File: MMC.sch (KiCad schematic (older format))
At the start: 53 parts, among them SW2 SW_Push, SW3 SW_Push, U2 LPC1776FET180,551, Y5 XTAL_8MHZ_TXC_7A-8.000MAAE-T

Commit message: DDR terminations changed, HTML BoM with variant added
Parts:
- C92, C93, Y5: config (none) -> dnf

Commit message: SW2 placement changed, BOM cleared, FPGA boot, less ERC errors and wornings
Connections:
- wire segments 245 -> 246
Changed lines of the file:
@@
 	8400 9600 8150 9600
 Wire Wire Line
-	8150 9600 8150 8100
+	8150 9600 8150 8800
 Wire Wire Line
 	8150 8100 8400 8100
@@
 	0    1    1    0
 $EndComp
+$Comp
+L power:PWR_FLAG #FLG?
+U 1 1 5D5D63E5
+P 8150 8800
+AR Path="/5BABAC65/5D5D63E5" Ref="#FLG?"  Part="1"
+AR Path="/5BCEDA39/5D5D63E5" Ref="#FLG0138"  Part="1"
+F 0 "#FLG0138" H 8150 8875 50  0001 C CNN
+F 1 "PWR_FLAG" H 8150 8973 50  0000 C CNN
+F 2 "" H 8150 8800 50  0001 C CNN
+F 3 "~" H 8150 8800 50  0001 C CNN
+	1    8150 8800
+	0    -1   -1   0
+$EndComp
+Connection ~ 8150 8800
+Wire Wire Line
+	8150 8800 8150 8100
+$Comp
+L power:PWR_FLAG #FLG?
+U 1 1 5D666D50
+P 8250 7900
+AR Path="/5BABAC65/5D666D50" Ref="#FLG?"  Part="1"
+AR Path="/5BCEDA39/5D666D50" Ref="#FLG0141"  Part="1"
+F 0 "#FLG0141" H 8250 7975 50  0001 C CNN
+F 1 "PWR_FLAG" H 8250 8073 50  0000 C CNN
+F 2 "" H 8250 7900 50  0001 C CNN
+F 3 "~" H 8250 7900 50  0001 C CNN
+	1    8250 7900
+	0    -1   -1   0
+$EndComp
 Wire Bus Line

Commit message: BOM updated, 25MHz clock level fixed
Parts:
- removed C92: CC0402_22PF_50V_5%_C0G, CAPC1005X55N, symbol Capacitors_SMD:CC0402_22PF_50V_5%_C0G
- added C92: CC0402_150PF_50V_5%_C0G, CAPC1005X55N, symbol Capacitors_SMD:CC0402_150PF_50V_5%_C0G
- R132: config (none) -> dnf
- SW3: value SW_Push -> KSS241GLFS
- U2: symbol AMC_FMC_Carrier-PcbDoc-rescue:LPC1776FET180,551-lpc1776fet180,551 -> AMC_FMC_Carrier-PcbDoc-rescue:LPC1776FET180,551-lpc1776fet180,551-AMC_FMC_Carrier-PcbDoc-rescue
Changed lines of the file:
@@
 $EndDescr
 $Comp
-L AMC_FMC_Carrier-PcbDoc-rescue:LPC1776FET180,551-lpc1776fet180,551 U?
+L AMC_FMC_Carrier-PcbDoc-rescue:LPC1776FET180,551-lpc1776fet180,551-AMC_FMC_Carrier-PcbDoc-rescue U?
 U 5 1 5BDFEB43
 P 8600 7800
@@
 $EndComp
 $Comp
-L AMC_FMC_Carrier-PcbDoc-rescue:LPC1776FET180,551-lpc1776fet180,551 U?
+L AMC_FMC_Carrier-PcbDoc-rescue:LPC1776FET180,551-lpc1776fet180,551-AMC_FMC_Carrier-PcbDoc-rescue U?
 U 1 1 5BE07B67
 P 4550 850
@@
 $EndComp
 $Comp
-L AMC_FMC_Carrier-PcbDoc-rescue:LPC1776FET180,551-lpc1776fet180,551 U?
+L AMC_FMC_Carrier-PcbDoc-rescue:LPC1776FET180,551-lpc1776fet180,551-AMC_FMC_Carrier-PcbDoc-rescue U?
 U 2 1 5BE0A46F
 P 13050 4700
@@
 $EndComp
 $Comp
-L AMC_FMC_Carrier-PcbDoc-rescue:LPC1776FET180,551-lpc1776fet180,551 U?
+L AMC_FMC_Carrier-PcbDoc-rescue:LPC1776FET180,551-lpc1776fet180,551-AMC_FMC_Carrier-PcbDoc-rescue U?
 U 4 1 5BE0D06F
 P 2750 8300
@@
 F 40 "Resistors SMD" H 2550 5780 60  0001 L CNN "Library Name"
 F 41 "This work is licensed under the Creative Commons CC-BY-SA 4.0 License. To the extent that circuit schematics that use Licensed Material can be considered to be ‘Adapted Material’, then the copyright holder waives article 3.b of the license with respect to these schematics." H 2550 5690 60  0001 L CNN "License"
+F 42 "dnf" V 2850 9650 50  0000 C CNN "config"
 	1    2550 9500
 	0    1    1    0
@@
 F 1 "SW_Push" H 10050 4944 50  0000 C CNN
 F 2 "Switches:PB_ALPS_SKHHLQA010" H 10050 4950 50  0001 C CNN
-F 3 "~" H 10050 4950 50  0001 C CNN
+F 3 "PB_ALPS_SKHHLQA010" H 10050 4950 50  0001 C CNN
 	1    10050 4750
 	1    0    0    -1
@@
 	3900 7150 4350 7150
 $Comp
-L AMC_FMC_Carrier-PcbDoc-rescue:LPC1776FET180,551-lpc1776fet180,551 U?
+L AMC_FMC_Carrier-PcbDoc-rescue:LPC1776FET180,551-lpc1776fet180,551-AMC_FMC_Carrier-PcbDoc-rescue U?
 U 3 1 5BE04771
 P 13050 650
@@
 NoConn ~ 12850 3450
 NoConn ~ 4350 6750
-$Comp
-L Switch:SW_Push SW?
-U 1 1 5CF2A4CC
-P 10050 5150
-AR Path="/5CF2A4CC" Ref="SW?"  Part="1"
-AR Path="/5BCEDA39/5CF2A4CC" Ref="SW3"  Part="1"
-F 0 "SW3" H 10050 5435 50  0000 C CNN
-F 1 "SW_Push" H 10050 5344 50  0000 C CNN
-F 2 "AG5300_2:KSS241GLFS" H 10050 5350 50  0001 C CNN
-F 3 "~" H 10050 5350 50  0001 C CNN
-	1    10050 5150
-	1    0    0    -1
-$EndComp
 Wire Wire Line
 	9850 4750 9850 5150
@@
 $EndComp
 $Comp
-L Capacitors_SMD:CC0402_22PF_50V_5%_C0G C92
-U 1 1 5CAC322E
+L power:PWR_FLAG #FLG?
+U 1 1 5D5D63E5
+P 8150 8800
+AR Path="/5BABAC65/5D5D63E5" Ref="#FLG?"  Part="1"
+AR Path="/5BCEDA39/5D5D63E5" Ref="#FLG0138"  Part="1"
+F 0 "#FLG0138" H 8150 8875 50  0001 C CNN
+F 1 "PWR_FLAG" H 8150 8973 50  0000 C CNN
+F 2 "" H 8150 8800 50  0001 C CNN
+F 3 "~" H 8150 8800 50  0001 C CNN
+	1    8150 8800
+	0    -1   -1   0
+$EndComp
+Connection ~ 8150 8800
+Wire Wire Line
+	8150 8800 8150 8100
+$Comp
+L power:PWR_FLAG #FLG?
+U 1 1 5D666D50
+P 8250 7900
+AR Path="/5BABAC65/5D666D50" Ref="#FLG?"  Part="1"
+AR Path="/5BCEDA39/5D666D50" Ref="#FLG0141"  Part="1"
+F 0 "#FLG0141" H 8250 7975 50  0001 C CNN
+F 1 "PWR_FLAG" H 8250 8073 50  0000 C CNN
+F 2 "" H 8250 7900 50  0001 C CNN
+F 3 "~" H 8250 7900 50  0001 C CNN
+	1    8250 7900
+	0    -1   -1   0
+$EndComp
+Wire Bus Line
+	11600 7200 11600 7400
+Wire Bus Line
+	12150 6100 12150 6400
+Wire Bus Line
+	10450 2900 10450 3650
+$Comp
+L Capacitors_SMD:CC0402_150PF_50V_5%_C0G C92
+U 1 1 5CFB3911
 P 1100 9550
 F 0 "C92" V 1204 9660 50  0000 L CNN
-F 1 "CC0402_22PF_50V_5%_C0G" H 1100 9290 60  0001 L CNN
+F 1 "CC0402_150PF_50V_5%_C0G" H 1100 9290 60  0001 L CNN
 F 2 "CAPC1005X55N" H 1100 8480 60  0001 L CNN
-F 3 "\\\\cern.ch\\dfs\\Applications\\Altium\\Datasheets\\CC0805_C0G_KEMET_(Commercial Grade).pdf" H 1100 9110 60  0001 L CNN
-F 4 "22pF" V 1295 9660 50  0000 L CNN "~"
-F 5 "CC0402_22PF_50V_5%_C0G" H 1100 9020 60  0001 L CNN "Part Number"
+F 3 "" H 1100 9110 60  0001 L CNN
+F 4 "150pF" V 1295 9660 50  0000 L CNN "~"
+F 5 "CC0402_150PF_50V_5%_C0G" H 1100 9020 60  0001 L CNN "Part Number"
 F 6 "Capacitor - non polarized" H 1100 8930 60  0001 L CNN "Library Ref"
 F 7 "SchLib\\Capacitors.SchLib" H 1100 8840 60  0001 L CNN "Library Path"
@@
 F 13 "CAPC1005X55N" H 1100 8210 60  0001 L CNN "Footprint Ref"
 F 14 "~~" H 1100 8120 60  0001 L CNN "PackageDescription"
-F 15 "22pF" H 1100 8030 60  0001 L CNN "Val"
+F 15 "150pF" H 1100 8030 60  0001 L CNN "Val"
 F 16 "Preferred" H 1100 7940 60  0001 L CNN "Status"
 F 17 "~~" H 1100 7850 60  0001 L CNN "Status Comment"
@@
 F 21 "SMD Multilayer Chip Ceramic Capacitor" H 1100 7490 60  0001 L CNN "Part Description"
 F 22 "GENERIC" H 1100 7400 60  0001 L CNN "Manufacturer"
-F 23 "CC0402_22PF_50V_5%_C0G" H 1100 7310 60  0001 L CNN "Manufacturer Part Number"
+F 23 "CC0402_150PF_50V_5%_C0G" H 1100 7310 60  0001 L CNN "Manufacturer Part Number"
 F 24 "0402" H 1100 7220 60  0001 L CNN "Case"
 F 25 "Yes" H 1100 7130 60  0001 L CNN "Mounted"
@@
 F 31 "~~" H 1100 6590 60  0001 L CNN "ComponentHeight"
 F 32 "KEMET" H 1100 6500 60  0001 L CNN "Manufacturer1 Example"
-F 33 "C0402C220J5GACTU" H 1100 6410 60  0001 L CNN "Manufacturer1 Part Number"
+F 33 "C0402C151J5GACTU" H 1100 6410 60  0001 L CNN "Manufacturer1 Part Number"
 F 34 "0.55mm" H 1100 6320 60  0001 L CNN "Manufacturer1 ComponentHeight"
 F 35 "\\\\cern.ch\\dfs\\Applications\\Altium\\Datasheets\\CC0805_C0G_KEMET_(Commercial Grade).pdf" H 1100 6230 60  0001 L CNN "HelpURL"
 F 36 "CERN DEM JLC" H 1100 6140 60  0001 L CNN "Author"
 F 37 "12/03/07 00:00:00" H 1100 6050 60  0001 L CNN "CreateDate"
-F 38 "12/03/07 00:00:00" H 1100 5960 60  0001 L CNN "LatestRevisionDate"
+F 38 "04/22/15 00:00:00" H 1100 5960 60  0001 L CNN "LatestRevisionDate"
 F 39 "Capacitors SMD" H 1100 5870 60  0001 L CNN "Library Name"
 F 40 "This work is licensed under the Creative Commons CC-BY-SA 4.0 License. To the extent that circuit schematics that use Licensed Material can be considered to be ‘Adapted Material’, then the copyright holder waives article 3.b of the license with respect to these schematics." H 1100 5780 60  0001 L CNN "License"
-F 41 "dnf" V 1400 9700 50  0000 C CNN "config"
 	1    1100 9550
 	0    1    1    0
 $EndComp
 $Comp
-L power:PWR_FLAG #FLG?
-U 1 1 5D5D63E5
-P 8150 8800
-AR Path="/5BABAC65/5D5D63E5" Ref="#FLG?"  Part="1"
-AR Path="/5BCEDA39/5D5D63E5" Ref="#FLG0138"  Part="1"
-F 0 "#FLG0138" H 8150 8875 50  0001 C CNN
-F 1 "PWR_FLAG" H 8150 8973 50  0000 C CNN
-F 2 "" H 8150 8800 50  0001 C CNN
-F 3 "~" H 8150 8800 50  0001 C CNN
-	1    8150 8800
-	0    -1   -1   0
-$EndComp
-Connection ~ 8150 8800
-Wire Wire Line
-	8150 8800 8150 8100
-$Comp
-L power:PWR_FLAG #FLG?
-U 1 1 5D666D50
-P 8250 7900
-AR Path="/5BABAC65/5D666D50" Ref="#FLG?"  Part="1"
-AR Path="/5BCEDA39/5D666D50" Ref="#FLG0141"  Part="1"
-F 0 "#FLG0141" H 8250 7975 50  0001 C CNN
-F 1 "PWR_FLAG" H 8250 8073 50  0000 C CNN
-F 2 "" H 8250 7900 50  0001 C CNN
-F 3 "~" H 8250 7900 50  0001 C CNN
-	1    8250 7900
-	0    -1   -1   0
+L Switch:SW_Push SW?
+U 1 1 5CF2A4CC
+P 10050 5150
+AR Path="/5CF2A4CC" Ref="SW?"  Part="1"
+AR Path="/5BCEDA39/5CF2A4CC" Ref="SW3"  Part="1"
+F 0 "SW3" H 10050 5435 50  0000 C CNN
+F 1 "KSS241GLFS" H 10050 5344 50  0001 C CNN
+F 2 "AG5300_2:KSS241GLFS" H 10050 5350 50  0001 C CNN
+F 3 "KSS241GLFS" H 10050 5350 50  0001 C CNN
+	1    10050 5150
+	1    0    0    -1
 $EndComp
-Wire Bus Line
-	11600 7200 11600 7400
-Wire Bus Line
-	12150 6100 12150 6400
-Wire Bus Line
-	10450 2900 10450 3650
 $EndSCHEMATC

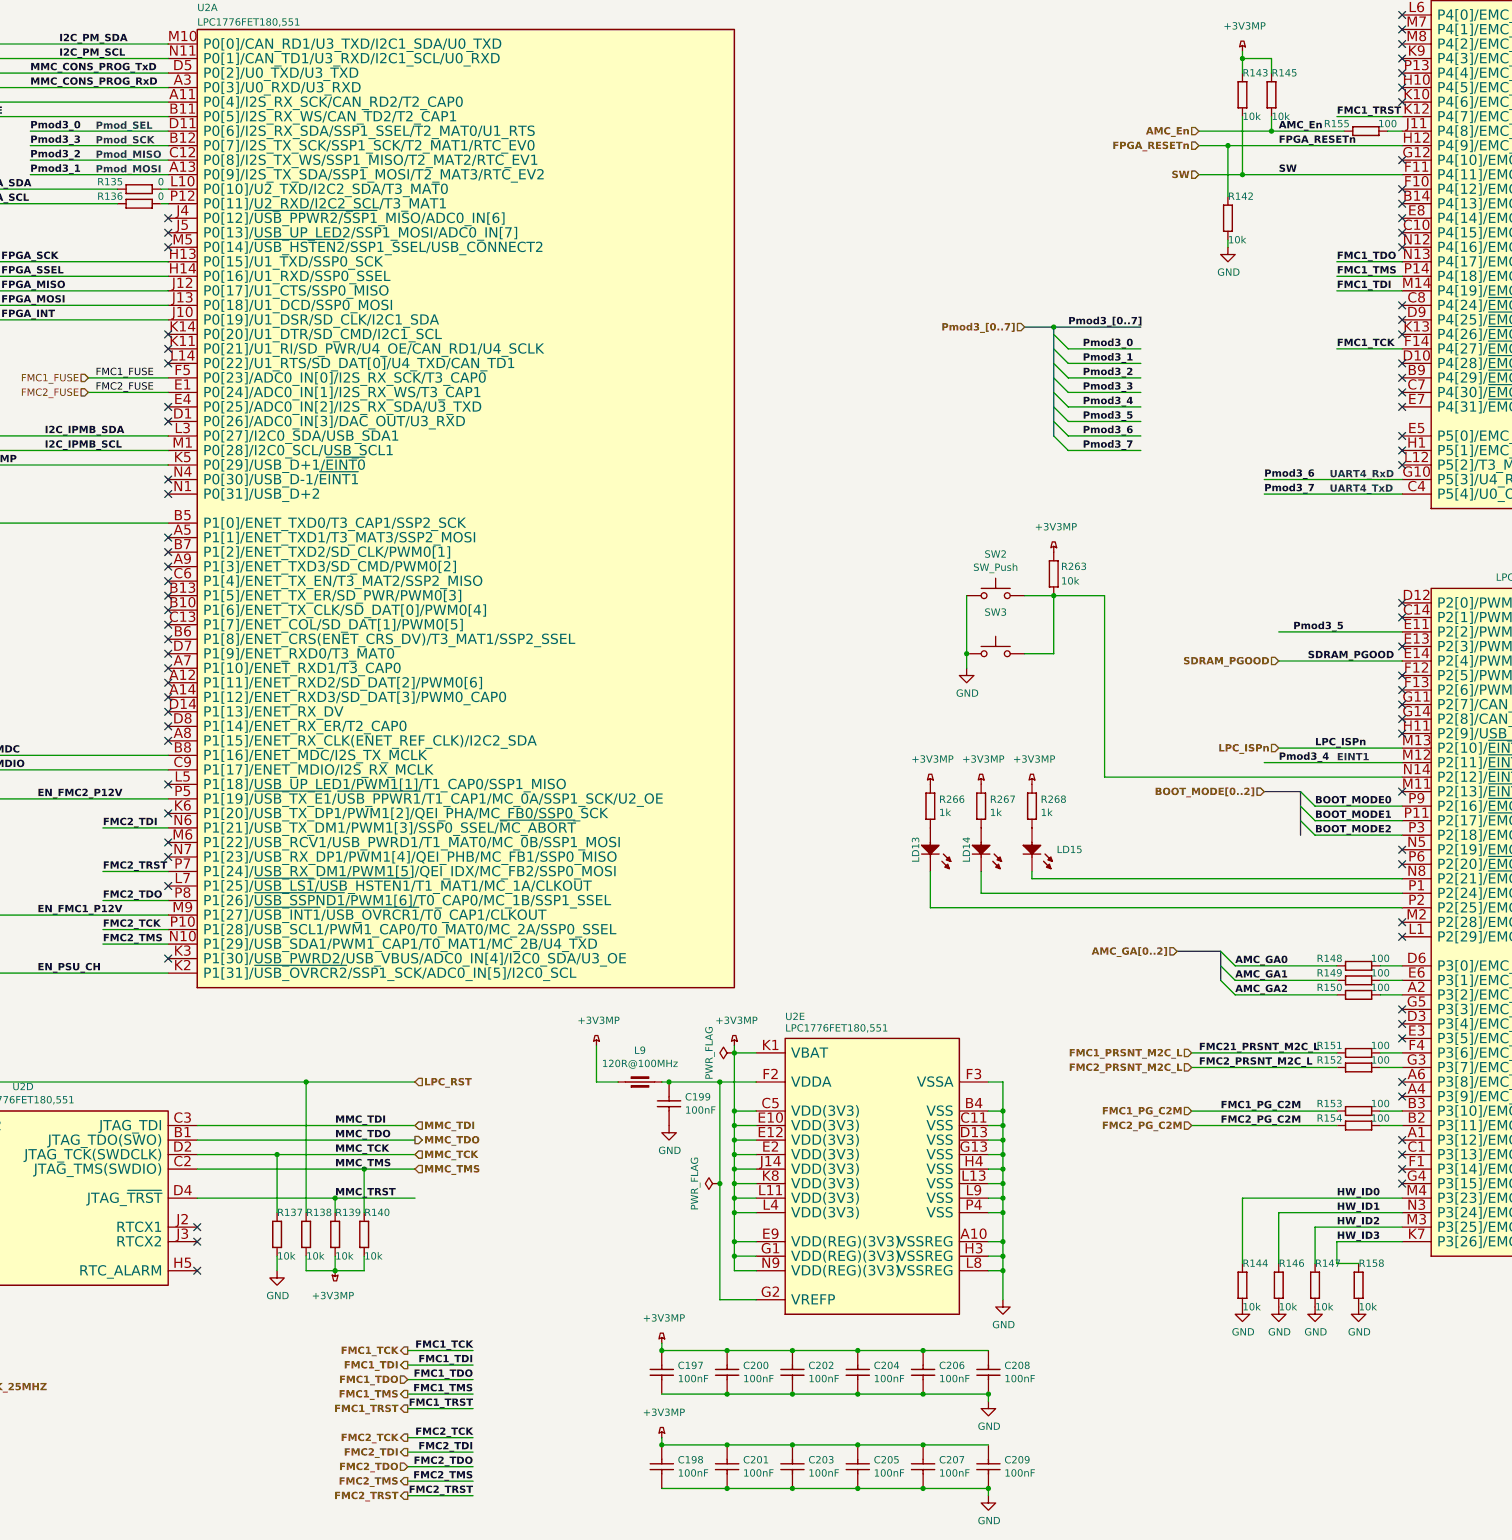
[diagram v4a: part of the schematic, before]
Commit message: new FMC JTAG chain connected to MMC GPIO
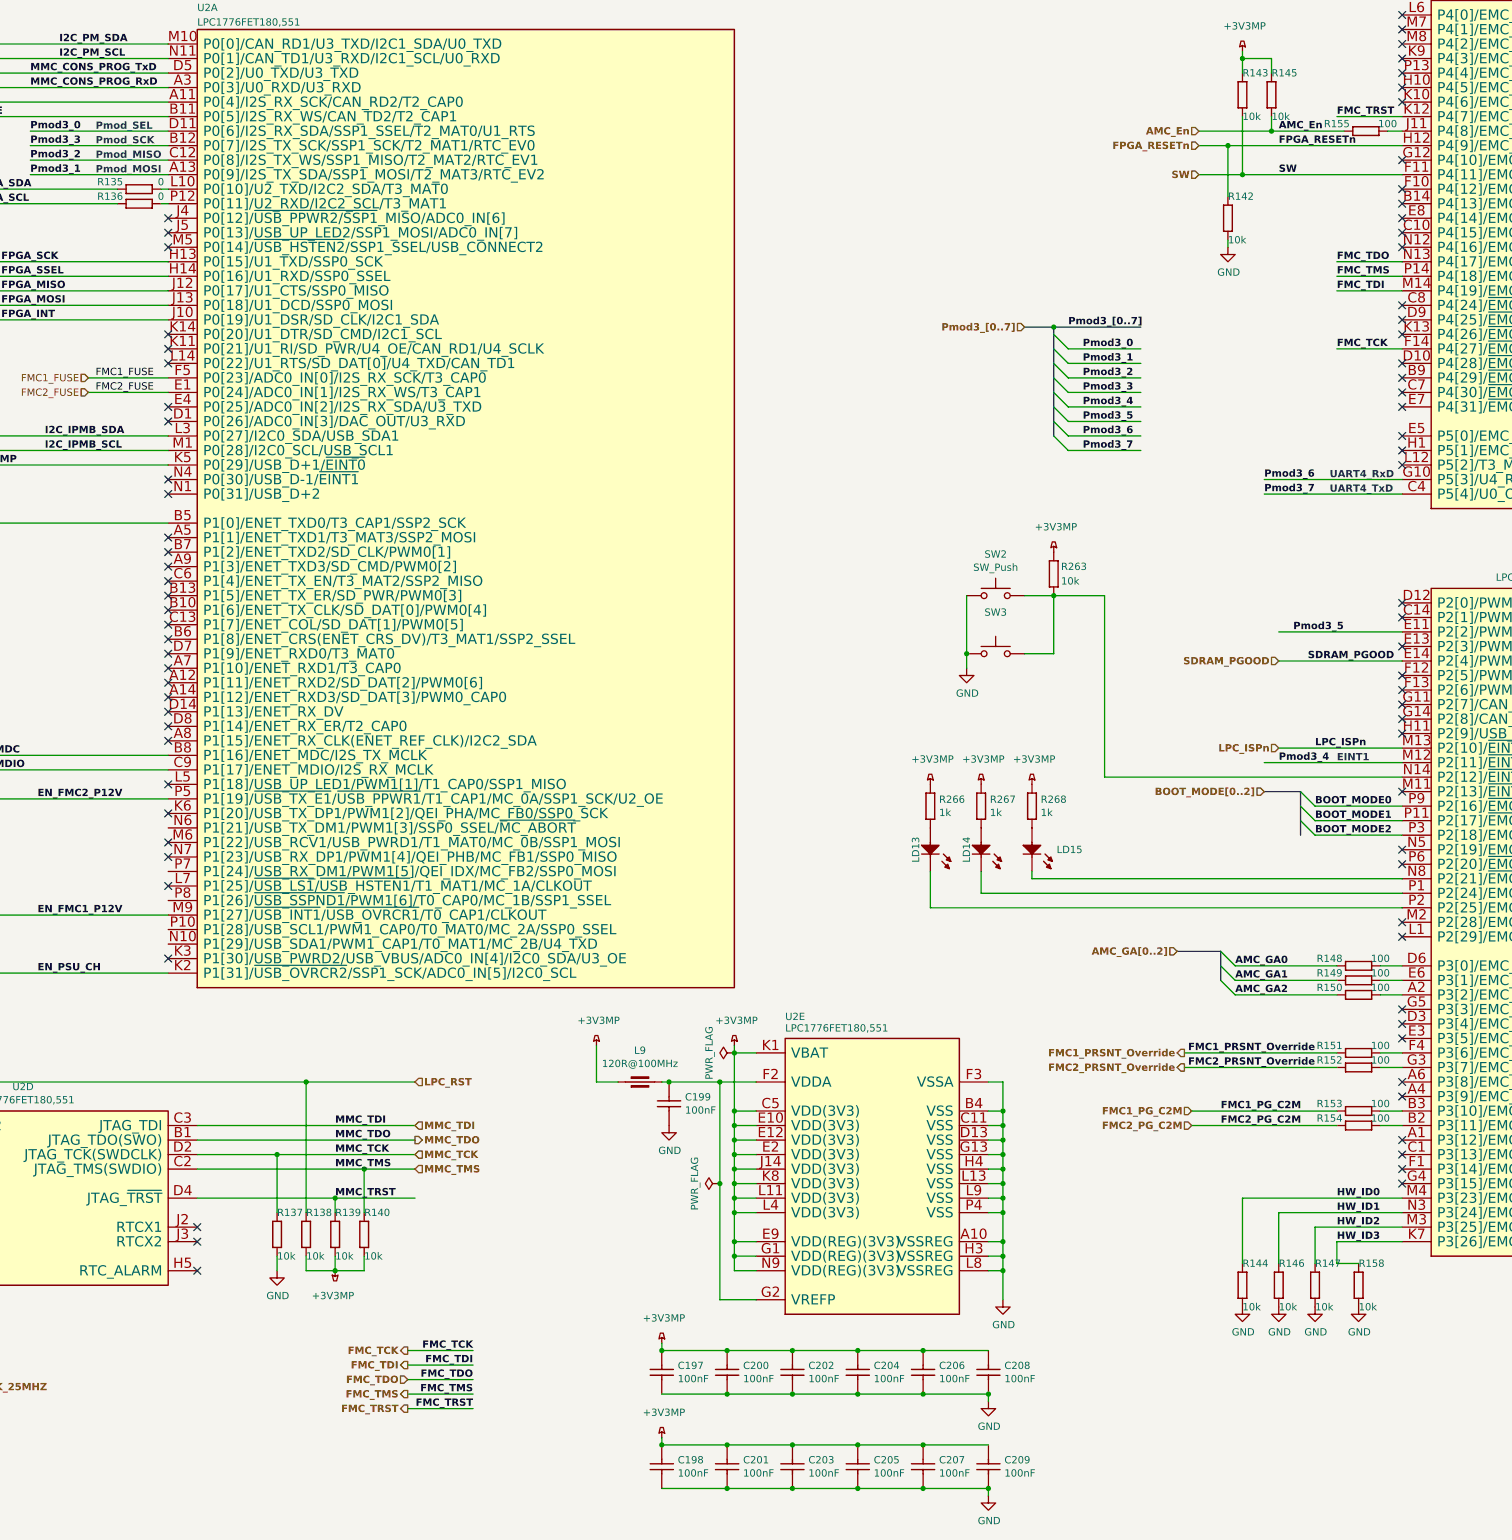
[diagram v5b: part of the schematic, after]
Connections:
- net labels added: FMC1_PRSNT_Override, FMC2_PRSNT_Override, FMC_TCK, FMC_TDI, FMC_TDO, FMC_TMS, FMC_TRST
- net labels removed: FMC1_PRSNT_M2C_L, FMC1_TCK, FMC1_TDI, FMC1_TDO, FMC1_TMS, FMC1_TRST, FMC21_PRSNT_M2C_L, FMC2_PRSNT_M2C_L, FMC2_TCK, FMC2_TDI, FMC2_TDO, FMC2_TMS, FMC2_TRST
- wire segments 246 -> 236
